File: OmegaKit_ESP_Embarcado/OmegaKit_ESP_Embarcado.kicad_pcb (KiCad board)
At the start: 2 copper layers, 2 x 7.5 mm, 20 parts, among them J1 USB_B_Micro, J2 MOTOR_B, J5 MOTOR_A, U1 CP2102N-Axx-xQFN28, U3 ESP32-WROOM-32, U5 AMS1117-3.3

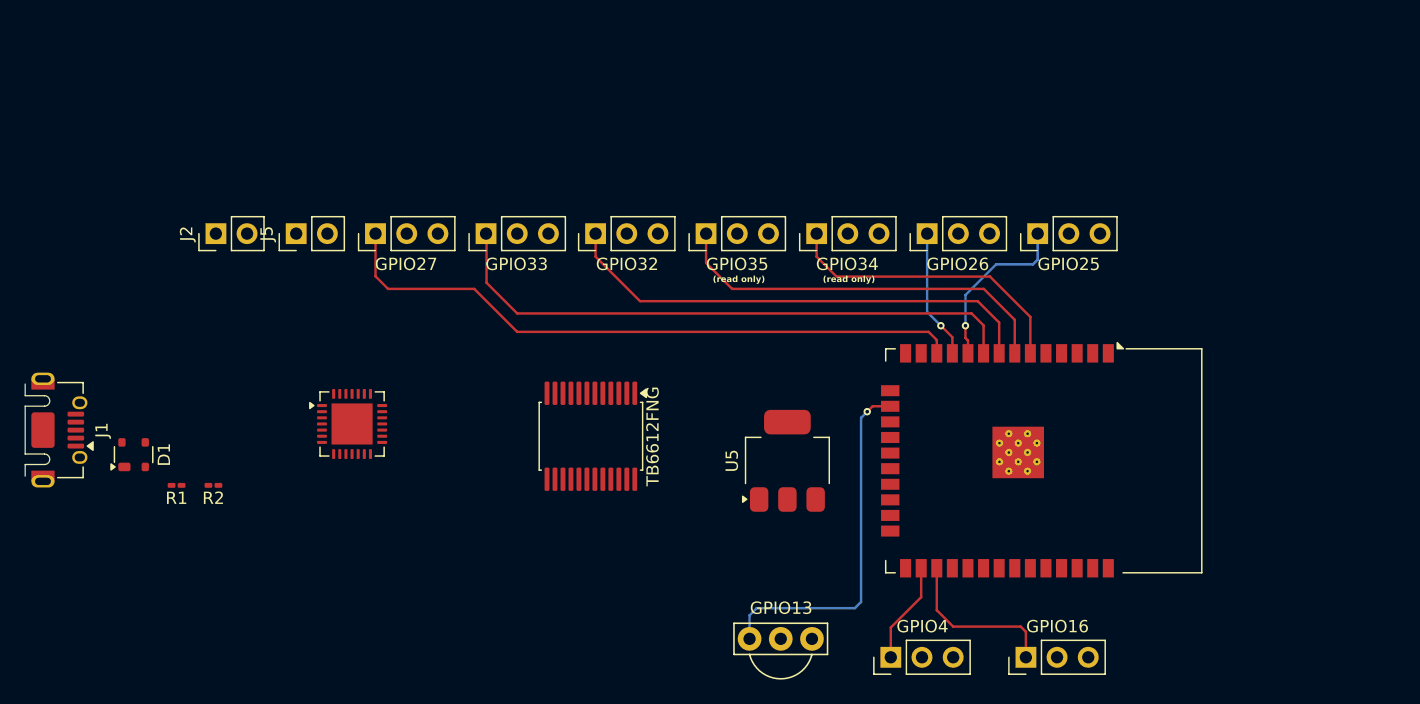
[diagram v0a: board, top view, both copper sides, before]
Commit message: ✨🚧 feat(Omegakit_ESP_Embarcado/*): Inicia desenho da PCB
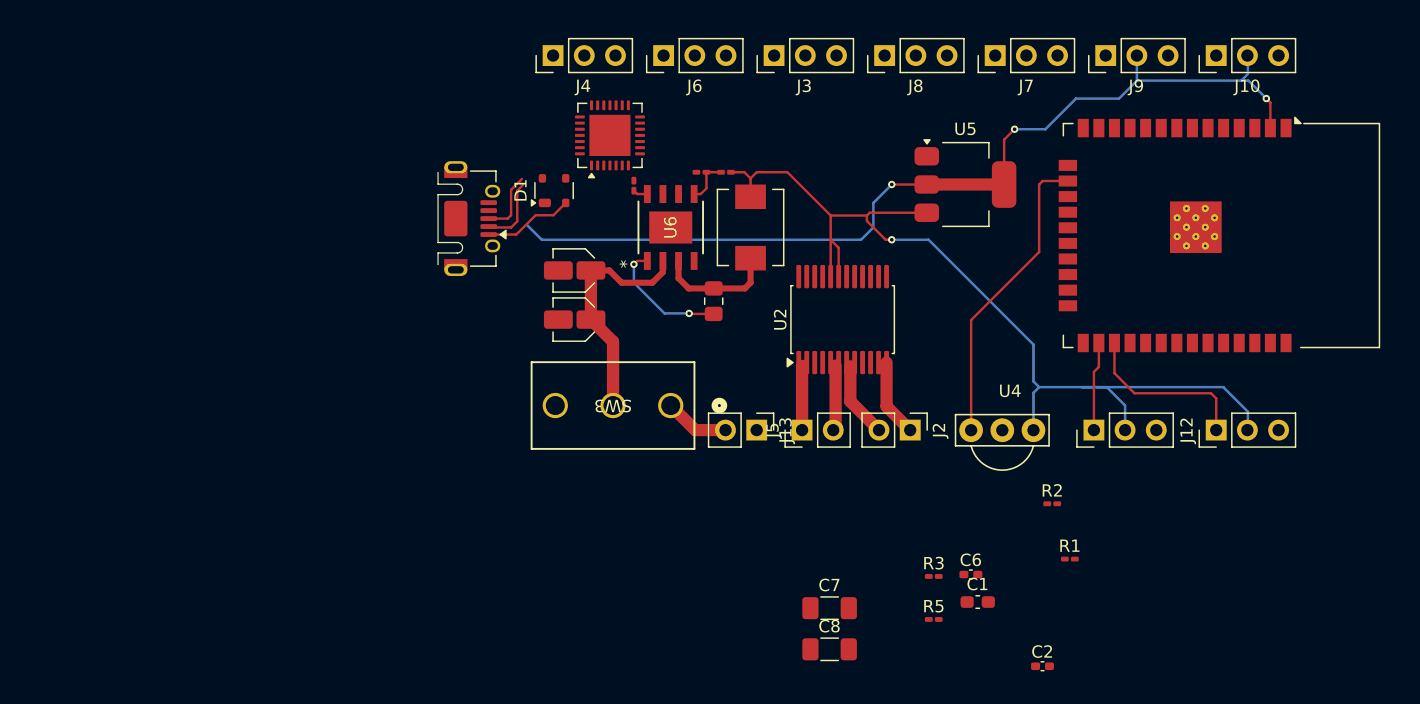
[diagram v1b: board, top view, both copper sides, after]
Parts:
- removed GPIO13: TSOP1838, TSOP1838:TSOP1838
- removed GPIO16: SERVO2, Connector_PinHeader_2.54mm:PinHeader_1x03_P2.54mm_Vertical
- removed GPIO25: QTR_1, Connector_PinHeader_2.54mm:PinHeader_1x03_P2.54mm_Vertical
- removed GPIO26: QTR_2, Connector_PinHeader_2.54mm:PinHeader_1x03_P2.54mm_Vertical
- removed GPIO27: SENSOR_1, Connector_PinHeader_2.54mm:PinHeader_1x03_P2.54mm_Vertical
- removed GPIO32: SENSOR_2, Connector_PinHeader_2.54mm:PinHeader_1x03_P2.54mm_Vertical
- removed GPIO33: SENSOR_3, Connector_PinHeader_2.54mm:PinHeader_1x03_P2.54mm_Vertical
- removed GPIO34: SENSOR_4, Connector_PinHeader_2.54mm:PinHeader_1x03_P2.54mm_Vertical
- removed GPIO35: SENSOR_5, Connector_PinHeader_2.54mm:PinHeader_1x03_P2.54mm_Vertical
- removed GPIO4: SERVO1, Connector_PinHeader_2.54mm:PinHeader_1x03_P2.54mm_Vertical
- removed TB6612FNG: TB6612FNG, Package_SO:SSOP-24_5.3x8.2mm_P0.65mm
- added C1: 100pF, Capacitor_SMD:C_0603_1608Metric_Pad1.08x0.95mm_HandSolder, F.Cu at (139.5, 85.5)
- added C2: 1uF, Capacitor_SMD:C_0402_1005Metric_Pad0.74x0.62mm_HandSolder, F.Cu at (144.8, 90.7)
- added C3: 10uF 25V, Capacitor_SMD:C_Elec_3x5.4, F.Cu at (106.7, 62.5)
- added C4: 10uF 25V, Capacitor_SMD:C_Elec_3x5.4, F.Cu at (106.7, 58.5)
- added C5: .1 uF, Capacitor_SMD:C_0201_0603Metric_Pad0.64x0.40mm_HandSolder, F.Cu at (111.5, 51.6)
- added C6: 3.9nF, Capacitor_SMD:C_0402_1005Metric_Pad0.74x0.62mm_HandSolder, F.Cu at (138.9, 83.3)
- added C7: 22uF 6.3V, Capacitor_SMD:C_1206_3216Metric_Pad1.33x1.80mm_HandSolder, F.Cu at (127.4, 86.0)
- added C8: 22uF 6.3V, Capacitor_SMD:C_1206_3216Metric_Pad1.33x1.80mm_HandSolder, F.Cu at (127.4, 89.3)
- added C9: 10nF, Capacitor_SMD:C_0805_2012Metric_Pad1.18x1.45mm_HandSolder, F.Cu at (118.0, 61.0)
- added J10: QTR_2, Connector_PinHeader_2.54mm:PinHeader_1x03_P2.54mm_Vertical, F.Cu at (158.9, 41.0)
- added J11: SERVO1, Connector_PinHeader_2.54mm:PinHeader_1x03_P2.54mm_Vertical, F.Cu at (149.0, 71.5)
- added J12: SERVO2, Connector_PinHeader_2.54mm:PinHeader_1x03_P2.54mm_Vertical, F.Cu at (158.9, 71.5)
- added J13: Conn_01x02_Socket, Connector_PinHeader_2.54mm:PinHeader_1x02_P2.54mm_Vertical, F.Cu at (121.5, 71.5)
- added J3: SENSOR_2, Connector_PinHeader_2.54mm:PinHeader_1x03_P2.54mm_Vertical, F.Cu at (122.9, 41.0)
- added J4: SENSOR_1, Connector_PinHeader_2.54mm:PinHeader_1x03_P2.54mm_Vertical, F.Cu at (104.9, 41.0)
- added J6: SENSOR_3, Connector_PinHeader_2.54mm:PinHeader_1x03_P2.54mm_Vertical, F.Cu at (113.9, 41.0)
- added J7: SENSOR_4, Connector_PinHeader_2.54mm:PinHeader_1x03_P2.54mm_Vertical, F.Cu at (140.9, 41.0)
- added J8: SENSOR_5, Connector_PinHeader_2.54mm:PinHeader_1x03_P2.54mm_Vertical, F.Cu at (131.9, 41.0)
- added J9: QTR_1, Connector_PinHeader_2.54mm:PinHeader_1x03_P2.54mm_Vertical, F.Cu at (149.9, 41.0)
- added L1: 10uH 4A (rever footprint, Inductor_SMD:L_Neosid_SM-PIC0512H, F.Cu at (121.0, 55.0)
- added R3: 6.8kOhm, Resistor_SMD:R_0201_0603Metric_Pad0.64x0.40mm_HandSolder, F.Cu at (135.9, 83.4)
- added R4: 10kOhm 1%, Resistor_SMD:R_0201_0603Metric_Pad0.64x0.40mm_HandSolder, F.Cu at (117.0, 50.5)
- added R5: 100kOhm, Resistor_SMD:R_0201_0603Metric_Pad0.64x0.40mm_HandSolder, F.Cu at (135.9, 86.9)
- added R6: 44.2kOhm 1% (corrigir), Resistor_SMD:R_0201_0603Metric_Pad0.64x0.40mm_HandSolder, F.Cu at (119.0, 50.5)
- added SW3: SS-12D10G5, footprints:SS-12D10G5_XKB, F.Cu at (114.5, 69.5)
- added U2: TB6612FNG, Package_SO:SSOP-24_5.3x8.2mm_P0.65mm, F.Cu at (128.5, 62.5)
- added U4: TSOP1838, TSOP1838:TSOP1838, F.Cu at (141.5, 71.5)
- added U6: MP2307DN-HW-LF-P, MP2307DN-HW-LF-P:IC8_MP2307_MNP, F.Cu at (114.5, 55.0)
- moved R1 73.0 mm to (147.0, 82.0), turned to 0 degrees
- moved R2 68.3 mm to (145.6, 77.5), turned to 0 degrees
- moved J2 58.8 mm to (134.0, 71.5), turned to -90 degrees
- moved J5 44.2 mm to (125.2, 71.5)
- moved D1 40.4 mm to (105.0, 52.0)
- moved J1 37.8 mm to (96.7, 54.3)
- moved U1 31.5 mm to (109.5, 47.5), turned to 90 degrees
- moved U5 26.8 mm to (138.5, 51.5), turned to 0 degrees
- moved U3 23.4 mm to (156.4, 55.7)
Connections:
- J2 pad 1: B01 -> BO1
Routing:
- net 5V: track 0.00 -> 78.7 mm, vias 0 -> 1
- net 3V3: track 0.11 -> 76.9 mm, vias 0 -> 3
- net SENSOR1: track 52.4 -> 0.00 mm
- net SENSOR3: track 48.2 -> 0.00 mm
- net SENSOR2: track 39.5 -> 0.00 mm
- net SENSOR5: track 32.2 -> 0.00 mm
- net 12V: track 0.00 -> 24.6 mm
- net SENSOR4: track 24.3 -> 0.00 mm
- net QTR1: track 14.0 -> 0.00 mm, vias 1 -> 0
- net QTR2: track 10.6 -> 0.00 mm, vias 1 -> 0
- net BS: track 0.00 -> 10.3 mm, vias 0 -> 2
- net SW: track 0.00 -> 9.81 mm
- net VBUS: track 0.00 -> 7.34 mm
- net BO1: track 0.00 -> 6.30 mm
- net BO2: track 0.00 -> 6.17 mm
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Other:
- outline, holes or cut-outs redrawn
- board text removed: "(read only)"

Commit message: ✨🚧 feat(OmegaKit_ESP_Embarcado/*): Monta primeira versão da placa, revisa circuitos, remove CP2102
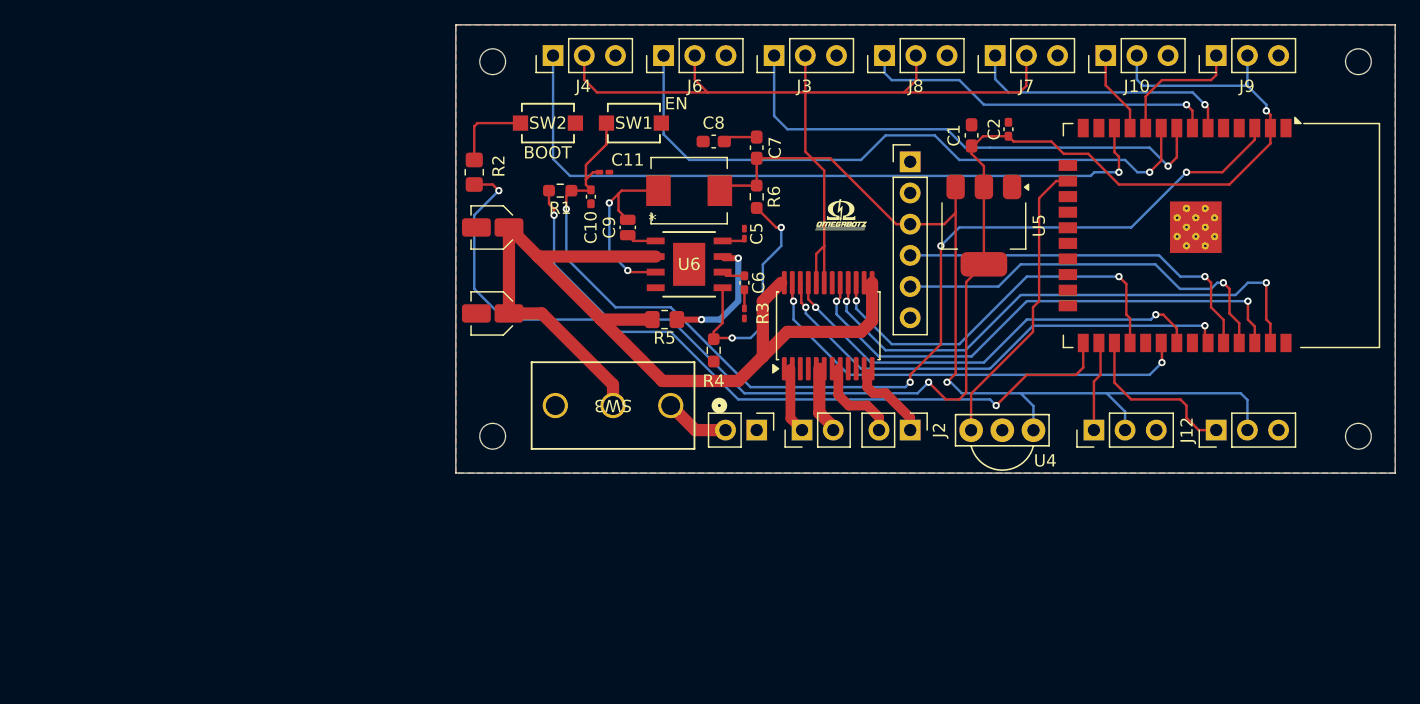
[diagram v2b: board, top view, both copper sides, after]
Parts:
- removed D1: SP0503BAHT, Package_TO_SOT_SMD:SOT-143
- removed J1: USB_B_Micro, Connector_USB:USB_Micro-AB_Molex_47590-0001
- removed U1: CP2102N-Axx-xQFN28, Package_DFN_QFN:QFN-28-1EP_5x5mm_P0.5mm_EP3.35x3.35mm
- added C10: 1uF, Capacitor_SMD:C_0402_1005Metric_Pad0.74x0.62mm_HandSolder, F.Cu at (108.0, 52.5)
- added C11: 100 nF, Capacitor_SMD:C_0201_0603Metric_Pad0.64x0.40mm_HandSolder, F.Cu at (109.1, 50.5)
- added REF**: MountingHole_2.1mm, MountingHole:MountingHole_2.1mm, F.Cu at (170.5, 72.0)
- added REF**: MountingHole_2.1mm, MountingHole:MountingHole_2.1mm, F.Cu at (100.0, 72.0)
- added REF**: MountingHole_2.1mm, MountingHole:MountingHole_2.1mm, F.Cu at (170.5, 41.5)
- added REF**: MountingHole_2.1mm, MountingHole:MountingHole_2.1mm, F.Cu at (100.0, 41.5)
- added SW1: TS-1088-AR02016, TS-1088-AR02016:SW_TS-1088_XNP, F.Cu at (111.5, 46.5)
- added SW2: TS-1088-AR02016, TS-1088-AR02016:SW_TS-1088_XNP, F.Cu at (104.5, 46.5)
- added UART_SOCKET1: Conn_01x06_Socket, Connector_PinHeader_2.54mm:PinHeader_1x06_P2.54mm_Vertical, F.Cu at (134.0, 49.6)
- C7, C8: footprint Capacitor_SMD:C_1206_3216Metric_Pad1.33x1.80mm_HandSolder -> Capacitor_SMD:C_0603_1608Metric_Pad1.08x0.95mm_HandSolder
- C9: footprint Capacitor_SMD:C_0805_2012Metric_Pad1.18x1.45mm_HandSolder -> Capacitor_SMD:C_0504_1310Metric_Pad0.83x1.28mm_HandSolder
- R1: value 22.1kOhm -> 10kOhm; footprint Resistor_SMD:R_0201_0603Metric_Pad0.64x0.40mm_HandSolder -> Resistor_SMD:R_0603_1608Metric_Pad0.98x0.95mm_HandSolder
- R2: value 47.5kOhm -> 100Ohm; footprint Resistor_SMD:R_0201_0603Metric_Pad0.64x0.40mm_HandSolder -> Resistor_SMD:R_0805_2012Metric_Pad1.20x1.40mm_HandSolder
- R4, R6: footprint Resistor_SMD:R_0201_0603Metric_Pad0.64x0.40mm_HandSolder -> Resistor_SMD:R_0603_1608Metric_Pad0.98x0.95mm_HandSolder
- R5: footprint Resistor_SMD:R_0201_0603Metric_Pad0.64x0.40mm_HandSolder -> Resistor_SMD:R_0805_2012Metric_Pad1.20x1.40mm_HandSolder
- moved R2 54.3 mm to (98.5, 50.5), turned to 90 degrees
- moved R1 51.2 mm to (105.5, 52.0), turned to 180 degrees
- moved C2 43.8 mm to (142.0, 47.0), turned to 90 degrees
- moved C8 42.4 mm to (118.0, 48.0), turned to 180 degrees
- moved C1 38.0 mm to (139.0, 47.5), turned to 90 degrees
- moved C7 38.0 mm to (121.5, 48.5), turned to 90 degrees
- moved R5 32.8 mm to (114.0, 62.5)
- moved C6 30.1 mm to (120.5, 59.5), turned to -90 degrees
- moved R3 26.4 mm to (120.5, 62.0), turned to 90 degrees
- moved R4 14.5 mm to (118.0, 65.0), turned to 90 degrees
- moved C5 9.81 mm to (120.5, 55.5)
- moved C9 9.22 mm to (111.0, 55.0)
- moved J10 9.00 mm to (149.9, 41.0)
- moved J9 9.00 mm to (158.9, 41.0)
- moved C4 7.54 mm to (100.0, 55.0)
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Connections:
- R1 pad 1: Net-(U1-VBUS) -> ESP_ENABLE
- R1 pad 2: VBUS -> 3V3
- R2 pad 1: GND -> BOOT
- R2 pad 2: Net-(U1-VBUS) -> Net-(R2-Pad2)
- U3 pad 25: unconnected-(U3-IO0-Pad25) -> BOOT
- U3 pad 28: PWMA -> PWMB
- U3 pad 30: PWMB -> PWMA
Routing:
- net ESP_ENABLE: track 0.00 -> 89.7 mm, vias 0 -> 4
- net BOOT: track 0.00 -> 67.8 mm, vias 0 -> 2
- net 5V: track 78.7 -> 145.5 mm
- net 12V: track 24.6 -> 85.1 mm
- net SENSOR1: track 0.00 -> 58.9 mm, vias 0 -> 1
- net SENSOR3: track 0.00 -> 52.9 mm, vias 0 -> 1
- net BIN2: track 0.00 -> 45.2 mm, vias 0 -> 2
- net BIN1: track 0.00 -> 43.2 mm, vias 0 -> 2
- net SENSOR2: track 0.00 -> 42.2 mm, vias 0 -> 1
- net AIN2: track 0.00 -> 40.0 mm, vias 0 -> 2
- net PWMA: track 0.00 -> 37.1 mm, vias 0 -> 2
- net AIN1: track 0.00 -> 36.8 mm, vias 0 -> 2
- net 3V3: track 76.9 -> 113.4 mm
- net PWMB: track 0.00 -> 32.8 mm, vias 0 -> 2
- net RX_CP2102: track 0.00 -> 32.7 mm, vias 0 -> 1
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- added copper zone on B.Cu, net GND
- added copper zone on F.Cu, net GND
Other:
- board size 2 x 7.5 mm -> 76.5 x 36.5 mm
- board text added: "BOOT"
- board text added: "EN"

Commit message: ✨ feat(OmegaKit_ESP_Embarcado/*): Adiciona LEDs nos sensores e LED de energia, muda footprint dos capacitores da bateria
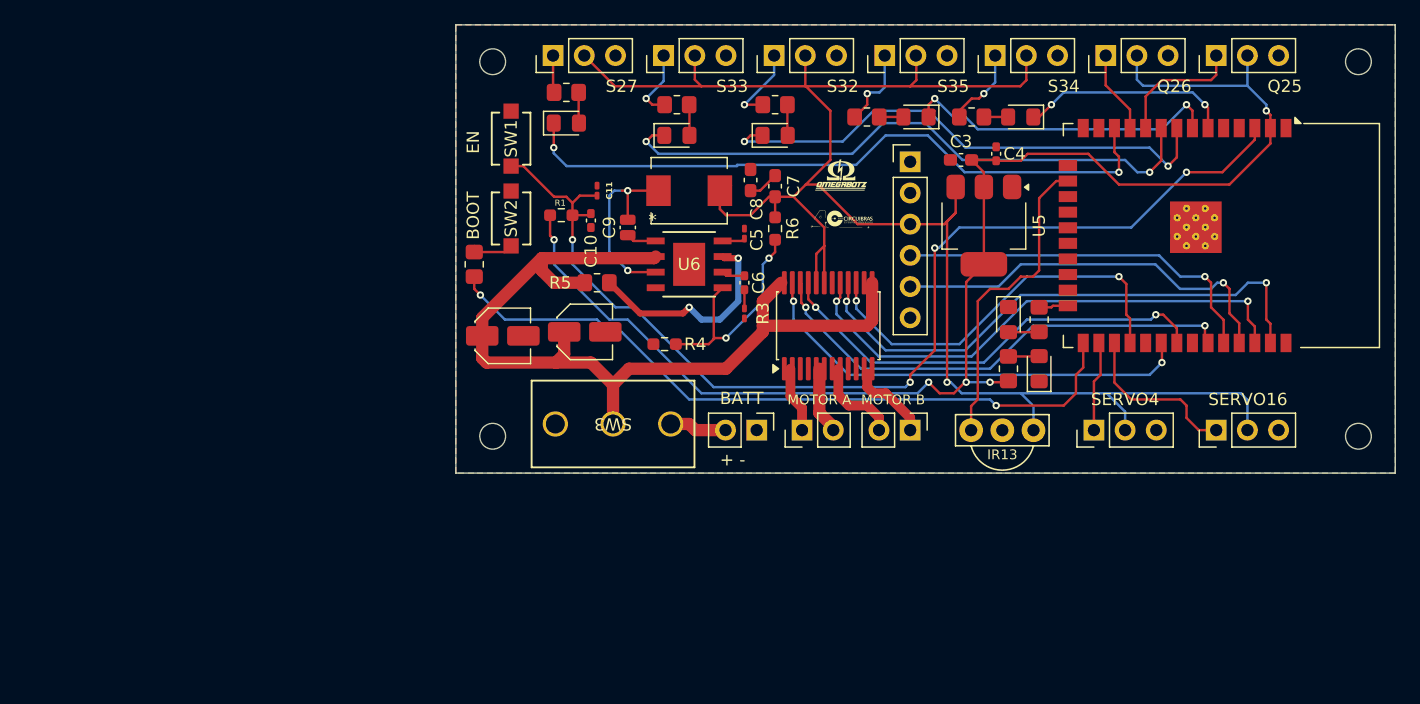
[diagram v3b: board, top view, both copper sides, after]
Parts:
- added D1: LED, LED_SMD:LED_0805_2012Metric_Pad1.15x1.40mm_HandSolder, F.Cu at (142.0, 62.5)
- added D2: LED, LED_SMD:LED_0805_2012Metric_Pad1.15x1.40mm_HandSolder, F.Cu at (106.0, 46.5)
- added D3: LED, LED_SMD:LED_0805_2012Metric_Pad1.15x1.40mm_HandSolder, F.Cu at (134.5, 46.0)
- added D4: LED, LED_SMD:LED_0805_2012Metric_Pad1.15x1.40mm_HandSolder, F.Cu at (123.0, 47.5)
- added D5: LED, LED_SMD:LED_0805_2012Metric_Pad1.15x1.40mm_HandSolder, F.Cu at (143.0, 46.0)
- added D6: LED, LED_SMD:LED_0805_2012Metric_Pad1.15x1.40mm_HandSolder, F.Cu at (115.0, 47.5)
- added D7: LED, LED_SMD:LED_0805_2012Metric_Pad1.15x1.40mm_HandSolder, F.Cu at (144.5, 66.5)
- added R10: 220Ohm, Resistor_SMD:R_0805_2012Metric_Pad1.20x1.40mm_HandSolder, F.Cu at (123.0, 45.0)
- added R11: 220Ohm, Resistor_SMD:R_0805_2012Metric_Pad1.20x1.40mm_HandSolder, F.Cu at (139.0, 46.0)
- added R12: 220Ohm, Resistor_SMD:R_0805_2012Metric_Pad1.20x1.40mm_HandSolder, F.Cu at (115.0, 45.0)
- added R13: 1KOhm, Resistor_SMD:R_0805_2012Metric_Pad1.20x1.40mm_HandSolder, F.Cu at (142.0, 66.5)
- added R7: 220Ohm, Resistor_SMD:R_0805_2012Metric_Pad1.20x1.40mm_HandSolder, F.Cu at (144.5, 62.5)
- added R8: 220Ohm, Resistor_SMD:R_0805_2012Metric_Pad1.20x1.40mm_HandSolder, F.Cu at (106.0, 44.0)
- added R9: 220Ohm, Resistor_SMD:R_0805_2012Metric_Pad1.20x1.40mm_HandSolder, F.Cu at (130.5, 46.0)
- C1: renamed from C3; footprint Capacitor_SMD:C_Elec_3x5.4 -> Capacitor_SMD:C_Elec_4x5.4
- C2: renamed from C4; footprint Capacitor_SMD:C_Elec_3x5.4 -> Capacitor_SMD:C_Elec_4x5.4
- moved SW1 10.1 mm to (101.5, 47.8), turned to 90 degrees
- moved C2 8.86 mm to (100.8, 63.8), turned to 0 degrees
- moved SW2 8.32 mm to (101.5, 54.3), turned to 90 degrees
- moved C1 7.65 mm to (107.5, 63.5), turned to 0 degrees
- moved R2 7.50 mm to (98.5, 58.0)
- moved R5 6.26 mm to (108.5, 59.5)
- moved C8 4.34 mm to (121.0, 51.1), turned to 90 degrees
- moved R4 4.03 mm to (114.0, 64.5), turned to 0 degrees
- moved C7 3.48 mm to (123.0, 51.6)
- moved R6 2.99 mm to (123.0, 55.1)
- moved C4 2.24 mm to (141.0, 49.0)
- moved C3 2.18 mm to (138.1, 49.5), turned to 180 degrees
- moved R1 2.00 mm to (105.6, 54.0)
- moved C10 1.93 mm to (108.0, 54.4)
- moved C11 1.61 mm to (108.5, 52.0), turned to 90 degrees
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- renumbered C1 to C3, C2 to C4, U4 to IR13, J9 to Q25, J10 to Q26, J4 to S27, J3 to S32, J6 to S33, J7 to S34, J8 to S35, J12 to SERVO16, J11 to SERVO4
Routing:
- net BOOT: track 67.8 -> 58.7 mm
- net 12V: track 85.1 -> 77.4 mm
- net EN_REG: track 10.5 -> 17.6 mm
- net SENSOR2: track 42.2 -> 49.1 mm, vias 1 -> 3
- net SENSOR5: track 29.2 -> 33.4 mm, vias 1 -> 3
- net Net-(R2-Pad2): track 6.61 -> 3.71 mm
- net SENSOR3: track 52.9 -> 55.6 mm, vias 1 -> 3
- net Net-(D6-A): track 0.00 -> 2.51 mm
- net Net-(D4-A): track 0.00 -> 2.51 mm
- net Net-(D2-A): track 0.00 -> 2.51 mm
- net Net-(D7-A): track 0.00 -> 2.51 mm
- net Net-(D1-A): track 0.00 -> 2.51 mm
- net LED_ONBOARD: track 0.00 -> 2.39 mm
- net Net-(D5-A): track 0.00 -> 1.97 mm
- net Net-(D3-A): track 0.00 -> 1.97 mm
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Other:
- board text added: "+ -"
- board text added: "BATT"
- board text added: "MOTOR A"
- board text added: "MOTOR B"
